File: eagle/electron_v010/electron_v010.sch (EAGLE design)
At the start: 91 parts, among them J1 SIM-NANO-4FF, J2 IPEX-20279-001E, U1 U-BLOX-SARA-U260, U2 SN74AVC4T245, U3 STM32F205RG, U4 MAX1704X, U5 SN74LVC1G07, U6 SN74LVC1G07, U8 SN74AVC4T245, X1 USB-MICROB, Y1 32Khz, Y2 26Mhz

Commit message: #8 Updated 3.3V regulator's inductor package footprint
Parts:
- U$6: device SparkFun-Passives:INDUCTOR0805 -> Particle:INDUCTORG
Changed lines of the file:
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@@
 <part name="R19" library="Spark" deviceset="R-US_" device="" value="10K"/>
 <part name="C7" library="Spark" deviceset="C-US" device="" value="47nF"/>
-<part name="U$6" library="SparkFun-Passives" deviceset="INDUCTOR" device="0805" value="0.47uH"/>
+<part name="U$6" library="Particle" deviceset="INDUCTOR" device="G" value="0.47uH"/>
 <part name="C40" library="Bretts-Spark-Library" deviceset="C-US" device="0603" value="2.2uF"/>
 <part name="C41" library="Bretts-Spark-Library" deviceset="C-US" device="0603" value="2.2uF"/>

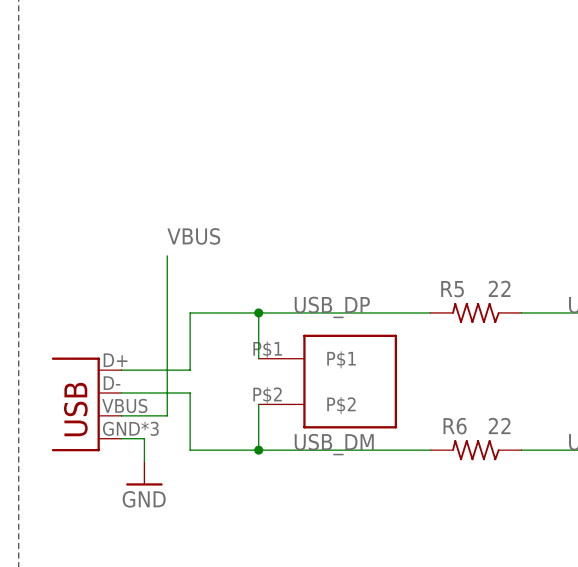
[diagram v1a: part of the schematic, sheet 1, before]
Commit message: #4 USB 5V exposed via hexagonal pad on top right corner above 3V3 pin
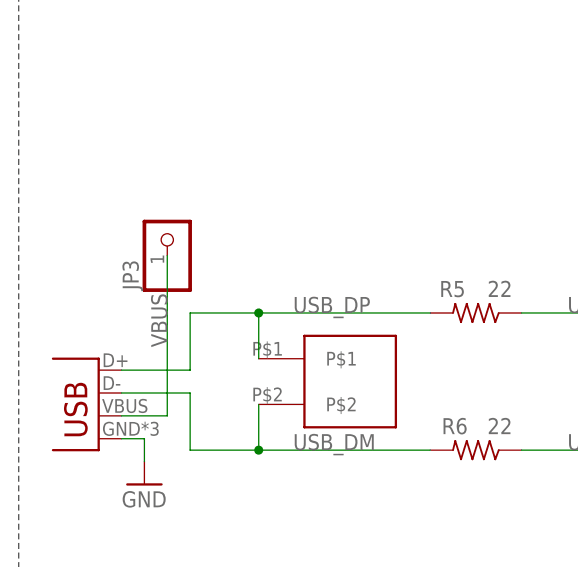
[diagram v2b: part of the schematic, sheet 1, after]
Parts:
- added JP3: (no value), pinhead:PINHD-1X1
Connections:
- net VBUS: now also JP3.1
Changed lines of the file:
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@@
 <setting verticaltext="up"/>
 </settings>
-<grid distance="0.1" unitdist="inch" unit="inch" style="lines" multiple="1" display="no" altdistance="0.01" altunitdist="inch" altunit="inch"/>
+<grid distance="0.05" unitdist="inch" unit="inch" style="lines" multiple="1" display="yes" altdistance="0.01" altunitdist="inch" altunit="inch"/>
 <layers>
 <layer number="1" name="Top" color="4" fill="1" visible="no" active="no"/>
@@
 <part name="U$7" library="Particle" deviceset="M02_0.05_HEADER" device=""/>
 <part name="C39" library="Spark" deviceset="C-US" device="" value="1uF"/>
+<part name="JP3" library="pinhead" deviceset="PINHD-1X1" device=""/>
 </parts>
 <sheets>
@@
 </instance>
 <instance part="U$7" gate="G$1" x="39.37" y="138.43"/>
+<instance part="JP3" gate="G$1" x="19.05" y="154.94" rot="R90"/>
 </instances>
 <busses>
@@
 <segment>
 <wire x1="13.97" y1="134.62" x2="19.05" y2="134.62" width="0.1524" layer="91"/>
-<label x="19.05" y="153.67" size="1.778" layer="95"/>
+<label x="19.05" y="142.24" size="1.778" layer="95" rot="R90"/>
 <pinref part="X1" gate="G$1" pin="VBUS"/>
 <wire x1="19.05" y1="134.62" x2="19.05" y2="152.4" width="0.1524" layer="91"/>
-</segment>
-<segment>
+<pinref part="JP3" gate="G$1" pin="1"/>
+</segment>
+<segment>

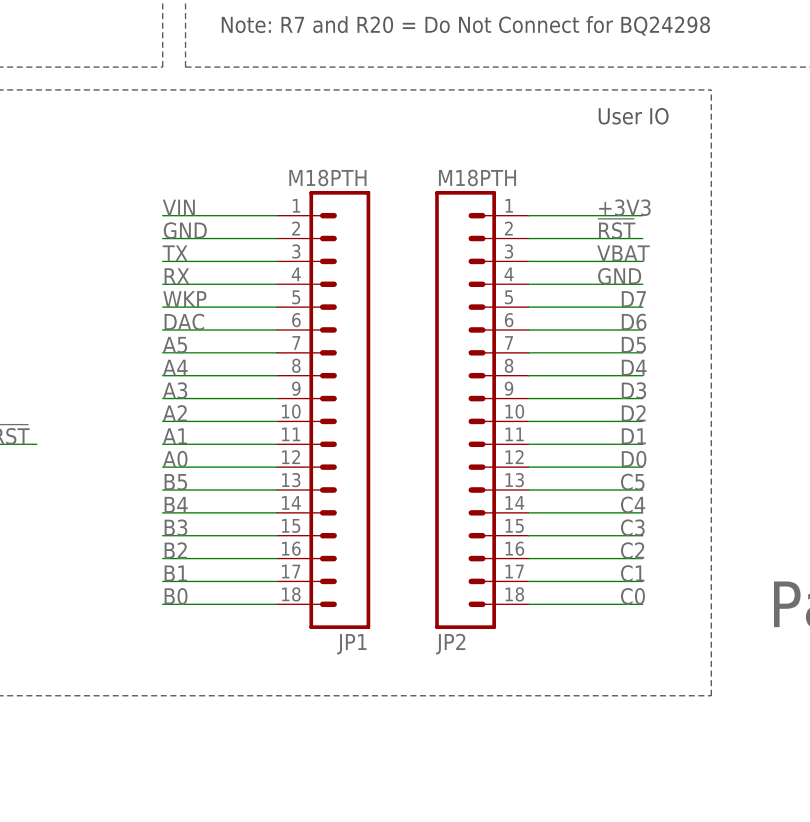
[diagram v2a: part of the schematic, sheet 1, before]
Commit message: #2 Replaced M18 round header pads with D-shaped pads and re-routed
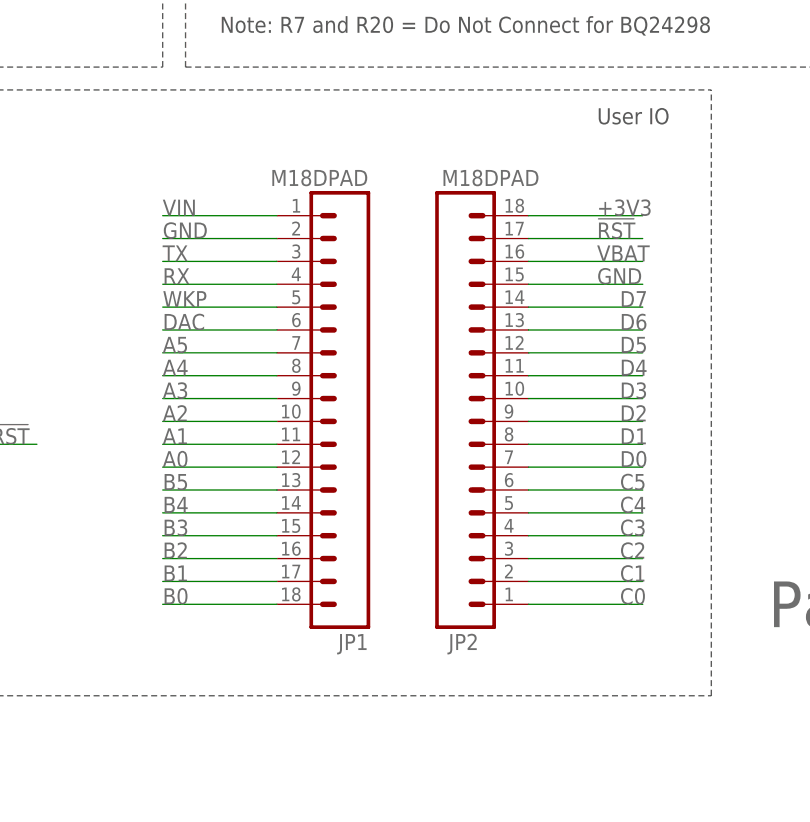
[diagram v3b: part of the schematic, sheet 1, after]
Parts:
- JP1, JP2: value M18PTH -> M18DPAD; device Bretts-Spark-Library:M18PTH -> Particle:M18DPAD
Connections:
- net !RST: now also JP2.17; no longer JP2.2
- net +3V3: now also JP2.18; no longer JP2.1
- net C0: now also JP2.1; no longer JP2.18
- net C1: now also JP2.2; no longer JP2.17
- net C2: now also JP2.3; no longer JP2.16
- net C3: now also JP2.4; no longer JP2.15
- net C4: now also JP2.5; no longer JP2.14
- net C5: now also JP2.6; no longer JP2.13
- net D0: now also JP2.7; no longer JP2.12
- net D1: now also JP2.8; no longer JP2.11
- net D2: now also JP2.9; no longer JP2.10
- net D3: now also JP2.10; no longer JP2.9
- net D4: now also JP2.11; no longer JP2.8
- net D5: now also JP2.12; no longer JP2.7
- net D6: now also JP2.13; no longer JP2.6
- net D7: now also JP2.14; no longer JP2.5
- net GND: now also JP2.15; no longer JP2.4
- net VBAT: now also JP2.16; no longer JP2.3
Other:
- moved on the sheet: JP2
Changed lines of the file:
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@@
 <part name="GND13" library="SparkFun" deviceset="GND" device=""/>
 <part name="C6" library="Spark" deviceset="C-US" device="" value="0.1uF"/>
-<part name="JP1" library="Bretts-Spark-Library" deviceset="M18" device="PTH" value="M18PTH"/>
-<part name="JP2" library="Bretts-Spark-Library" deviceset="M18" device="PTH" value="M18PTH"/>
+<part name="JP1" library="Particle" deviceset="M18" device="DPAD" value="M18DPAD"/>
 <part name="+3V16" library="supply1" deviceset="+3V3" device=""/>
 <part name="R10" library="Spark" deviceset="R-US_" device="" value="1K"/>
@@
 <part name="C39" library="Spark" deviceset="C-US" device="" value="1uF"/>
 <part name="JP3" library="pinhead" deviceset="PINHD-1X1" device=""/>
+<part name="JP2" library="Particle" deviceset="M18" device="DPAD"/>
 </parts>
 <sheets>
@@
 <attribute name="NAME" x="106.68" y="25.908" size="1.778" layer="95" rot="R180"/>
 </instance>
-<instance part="JP2" gate="G$1" x="116.84" y="52.07" smashed="yes" rot="MR180">
-<attribute name="VALUE" x="114.3" y="77.47" size="1.778" layer="96" rot="MR180"/>
-<attribute name="NAME" x="114.3" y="25.908" size="1.778" layer="95" rot="MR180"/>
-</instance>
 <instance part="+3V16" gate="G$1" x="187.96" y="83.82" smashed="yes">
 <attribute name="VALUE" x="185.42" y="78.74" size="1.778" layer="96" rot="R90"/>
@@
 <instance part="U$7" gate="G$1" x="39.37" y="138.43"/>
 <instance part="JP3" gate="G$1" x="19.05" y="154.94" rot="R90"/>
+<instance part="JP2" gate="G$1" x="116.84" y="49.53" smashed="yes">
+<attribute name="VALUE" x="114.808" y="75.692" size="1.778" layer="96"/>
+<attribute name="NAME" x="115.57" y="24.13" size="1.778" layer="95"/>
+</instance>
 </instances>
 <busses>
@@
 </segment>
 <segment>
-<pinref part="JP2" gate="G$1" pin="1"/>
 <wire x1="124.46" y1="72.39" x2="137.16" y2="72.39" width="0.1524" layer="91"/>
 <label x="132.08" y="72.39" size="1.778" layer="95"/>
+<pinref part="JP2" gate="G$1" pin="18"/>
 </segment>
 <segment>
@@
 </segment>
 <segment>
-<pinref part="JP2" gate="G$1" pin="2"/>
 <wire x1="124.46" y1="69.85" x2="137.16" y2="69.85" width="0.1524" layer="91"/>
 <label x="132.08" y="69.85" size="1.778" layer="95"/>
+<pinref part="JP2" gate="G$1" pin="17"/>
 </segment>
 </net>
@@
 </segment>
 <segment>
-<pinref part="JP2" gate="G$1" pin="4"/>
 <wire x1="124.46" y1="64.77" x2="137.16" y2="64.77" width="0.1524" layer="91"/>
 <label x="132.08" y="64.77" size="1.778" layer="95"/>
+<pinref part="JP2" gate="G$1" pin="15"/>
 </segment>
 <segment>
@@
 <net name="VBAT" class="0">
 <segment>
-<pinref part="JP2" gate="G$1" pin="3"/>
 <wire x1="124.46" y1="67.31" x2="137.16" y2="67.31" width="0.1524" layer="91"/>
 <label x="132.08" y="67.31" size="1.778" layer="95"/>
+<pinref part="JP2" gate="G$1" pin="16"/>
 </segment>
 </net>
 <net name="D7" class="0">
 <segment>
-<pinref part="JP2" gate="G$1" pin="5"/>
 <wire x1="124.46" y1="62.23" x2="137.16" y2="62.23" width="0.1524" layer="91"/>
 <label x="134.62" y="62.23" size="1.778" layer="95"/>
+<pinref part="JP2" gate="G$1" pin="14"/>
 </segment>
 <segment>
@@
 <net name="D6" class="0">
 <segment>
-<pinref part="JP2" gate="G$1" pin="6"/>
 <wire x1="124.46" y1="59.69" x2="137.16" y2="59.69" width="0.1524" layer="91"/>
 <label x="134.62" y="59.69" size="1.778" layer="95"/>
+<pinref part="JP2" gate="G$1" pin="13"/>
 </segment>
 </net>
 <net name="D5" class="0">
 <segment>
-<pinref part="JP2" gate="G$1" pin="7"/>
 <wire x1="124.46" y1="57.15" x2="137.16" y2="57.15" width="0.1524" layer="91"/>
 <label x="134.62" y="57.15" size="1.778" layer="95"/>
+<pinref part="JP2" gate="G$1" pin="12"/>
 </segment>
 </net>
 <net name="D4" class="0">
 <segment>
-<pinref part="JP2" gate="G$1" pin="8"/>
 <wire x1="124.46" y1="54.61" x2="137.16" y2="54.61" width="0.1524" layer="91"/>
 <label x="134.62" y="54.61" size="1.778" layer="95"/>
+<pinref part="JP2" gate="G$1" pin="11"/>
 </segment>
 </net>
 <net name="D3" class="0">
 <segment>
-<pinref part="JP2" gate="G$1" pin="9"/>
 <wire x1="124.46" y1="52.07" x2="137.16" y2="52.07" width="0.1524" layer="91"/>
 <label x="134.62" y="52.07" size="1.778" layer="95"/>
+<pinref part="JP2" gate="G$1" pin="10"/>
 </segment>
 </net>
 <net name="D2" class="0">
 <segment>
-<pinref part="JP2" gate="G$1" pin="10"/>
 <wire x1="124.46" y1="49.53" x2="137.16" y2="49.53" width="0.1524" layer="91"/>
 <label x="134.62" y="49.53" size="1.778" layer="95"/>
+<pinref part="JP2" gate="G$1" pin="9"/>
 </segment>
 </net>
 <net name="D1" class="0">
 <segment>
-<pinref part="JP2" gate="G$1" pin="11"/>
 <wire x1="124.46" y1="46.99" x2="137.16" y2="46.99" width="0.1524" layer="91"/>
 <label x="134.62" y="46.99" size="1.778" layer="95"/>
+<pinref part="JP2" gate="G$1" pin="8"/>
 </segment>
 </net>
 <net name="D0" class="0">
 <segment>
-<pinref part="JP2" gate="G$1" pin="12"/>
 <wire x1="124.46" y1="44.45" x2="137.16" y2="44.45" width="0.1524" layer="91"/>
 <label x="134.62" y="44.45" size="1.778" layer="95"/>
+<pinref part="JP2" gate="G$1" pin="7"/>
 </segment>
 </net>
 <net name="C5" class="0">
 <segment>
-<pinref part="JP2" gate="G$1" pin="13"/>
 <wire x1="124.46" y1="41.91" x2="137.16" y2="41.91" width="0.1524" layer="91"/>
 <label x="134.62" y="41.91" size="1.778" layer="95"/>
+<pinref part="JP2" gate="G$1" pin="6"/>
 </segment>
 </net>
 <net name="C4" class="0">
 <segment>
-<pinref part="JP2" gate="G$1" pin="14"/>
 <wire x1="124.46" y1="39.37" x2="137.16" y2="39.37" width="0.1524" layer="91"/>
 <label x="134.62" y="39.37" size="1.778" layer="95"/>
+<pinref part="JP2" gate="G$1" pin="5"/>
 </segment>
 </net>
 <net name="C3" class="0">
 <segment>
-<pinref part="JP2" gate="G$1" pin="15"/>
 <wire x1="124.46" y1="36.83" x2="137.16" y2="36.83" width="0.1524" layer="91"/>
 <label x="134.62" y="36.83" size="1.778" layer="95"/>
+<pinref part="JP2" gate="G$1" pin="4"/>
 </segment>
 </net>
 <net name="C2" class="0">
 <segment>
-<pinref part="JP2" gate="G$1" pin="16"/>
 <wire x1="124.46" y1="34.29" x2="137.16" y2="34.29" width="0.1524" layer="91"/>
 <label x="134.62" y="34.29" size="1.778" layer="95"/>
+<pinref part="JP2" gate="G$1" pin="3"/>
 </segment>
 </net>
 <net name="C1" class="0">
 <segment>
-<pinref part="JP2" gate="G$1" pin="17"/>
 <wire x1="124.46" y1="31.75" x2="137.16" y2="31.75" width="0.1524" layer="91"/>
 <label x="134.62" y="31.75" size="1.778" layer="95"/>
+<pinref part="JP2" gate="G$1" pin="2"/>
 </segment>
 </net>
 <net name="C0" class="0">
 <segment>
-<pinref part="JP2" gate="G$1" pin="18"/>
 <wire x1="124.46" y1="29.21" x2="137.16" y2="29.21" width="0.1524" layer="91"/>
 <label x="134.62" y="29.21" size="1.778" layer="95"/>
-</segment>
-</net>
+<pinref part="JP2" gate="G$1" pin="1"/>
+</segment>
+</net>
